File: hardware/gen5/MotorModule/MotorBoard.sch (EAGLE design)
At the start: 42 parts, among them J1 M20X2SHROUDED

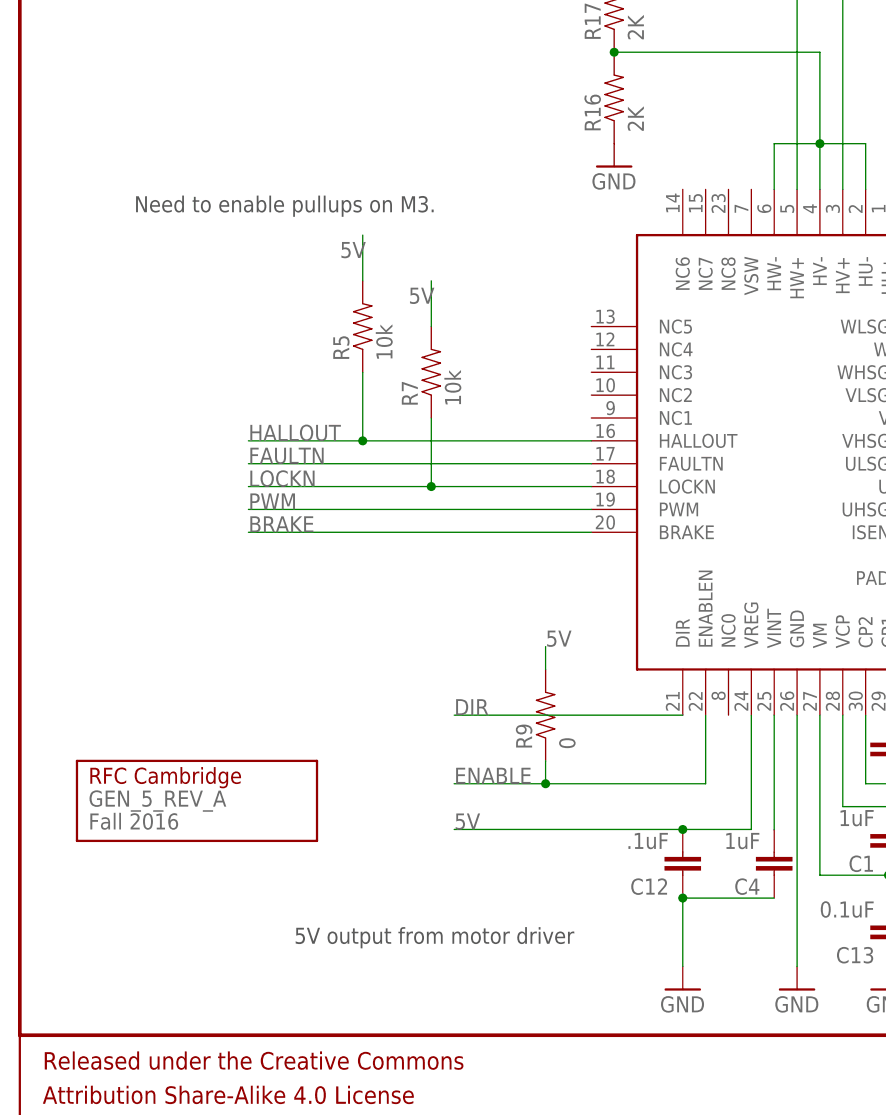
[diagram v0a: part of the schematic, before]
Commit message: added client code in rfc-ssl-vision-client
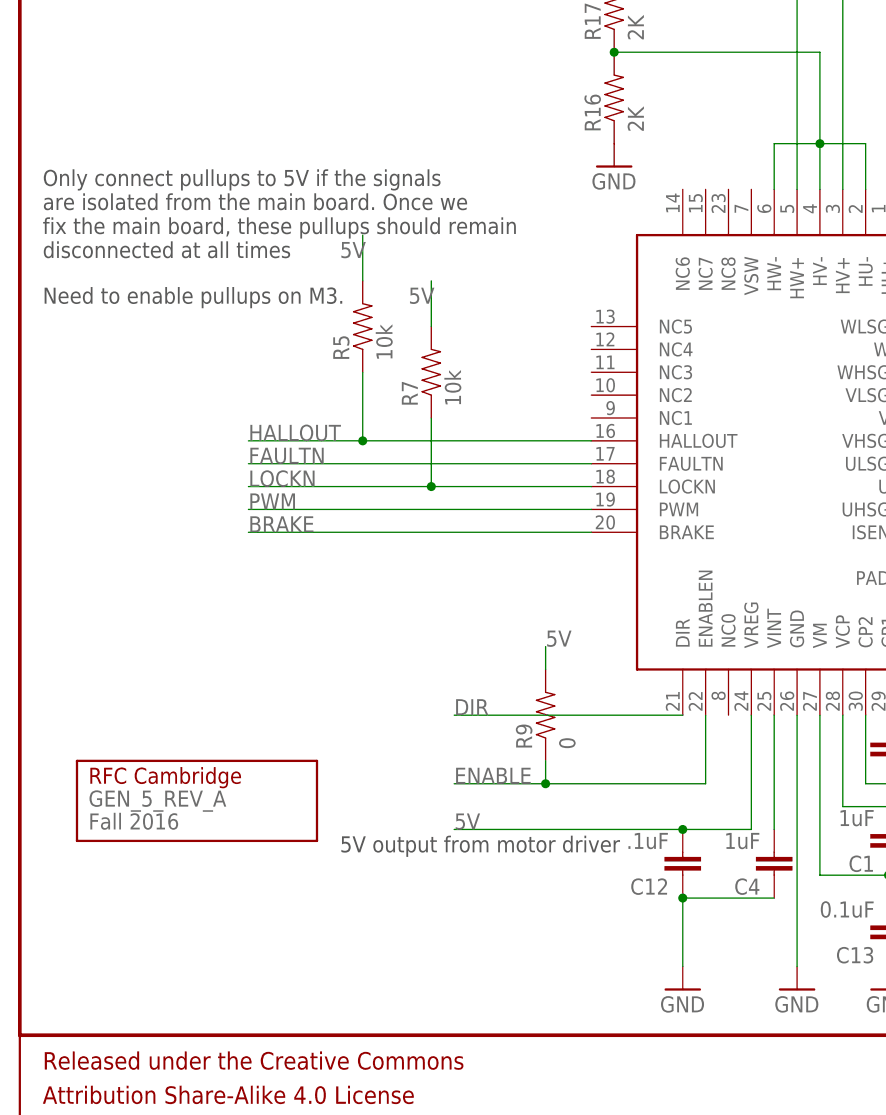
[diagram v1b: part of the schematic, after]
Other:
- note added: "Only connect pullups to 5V if the signals are isolated from the main board. Once we fix the main board, these pullups should remain disconnected at all times"
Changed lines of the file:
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@@
 <sheet>
 <plain>
-<text x="30.48" y="10.16" size="1.778" layer="97">5V output from motor driver</text>
+<text x="35.56" y="20.32" size="1.778" layer="97">5V output from motor driver</text>
 <text x="157.48" y="55.88" size="1.778" layer="97">Need to connect these with high current</text>
 <text x="157.48" y="53.34" size="1.778" layer="97">Separate connector?</text>
 <text x="254" y="81.28" size="1.778" layer="97">24, 26, and 30 are unconnected in Rev A</text>
-<text x="12.7" y="91.44" size="1.778" layer="97">Need to enable pullups on M3.</text>
+<text x="2.54" y="81.28" size="1.778" layer="97">Need to enable pullups on M3.</text>
+<text x="2.54" y="86.36" size="1.778" layer="97">Only connect pullups to 5V if the signals
+are isolated from the main board. Once we
+fix the main board, these pullups should remain
+disconnected at all times</text>
 </plain>
 <instances>
@@
 </schematic>
 </drawing>
+<compatibility>
+<note version="6.3" minversion="6.2.2" severity="warning">
+Since Version 6.2.2 text objects can contain more than one line,
+which will not be processed correctly with this version.
+</note>
+</compatibility>
 </eagle>

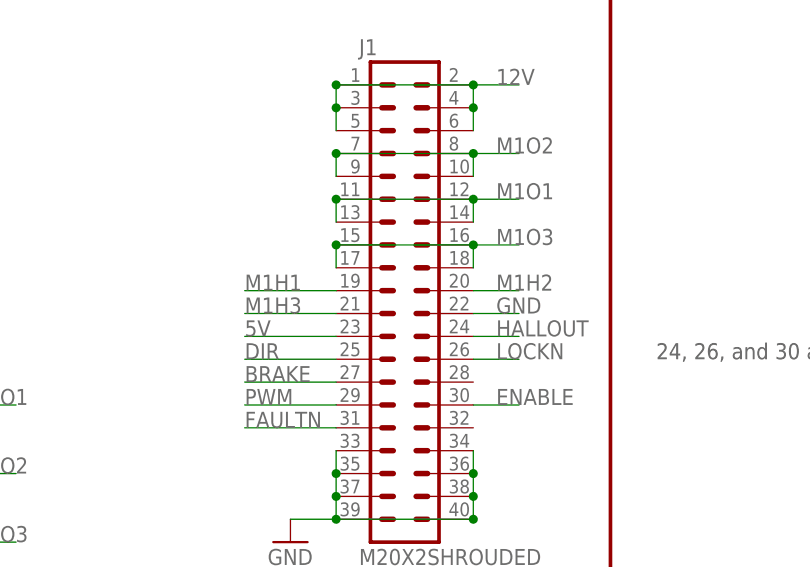
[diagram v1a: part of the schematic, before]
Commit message: swapped motorboard traces for hallout signals
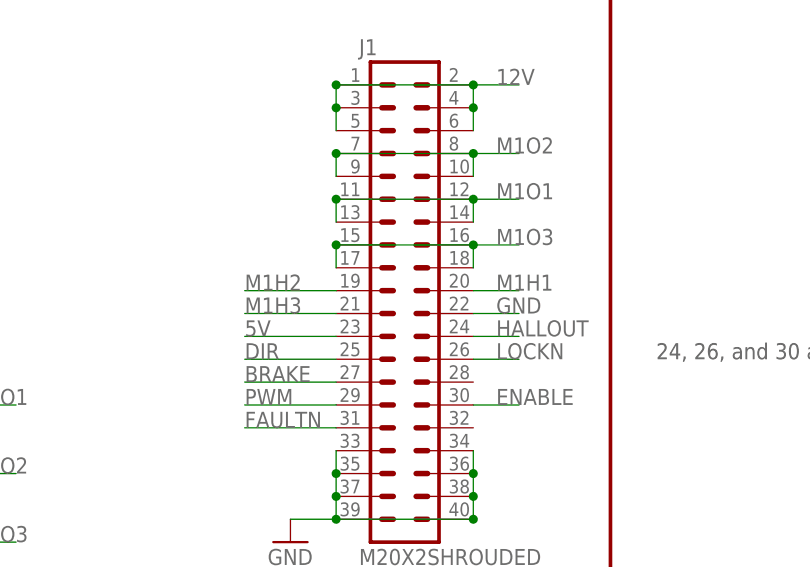
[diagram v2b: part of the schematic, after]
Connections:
- net M1H1: now also J1.20; no longer J1.19
- net M1H2: now also J1.19; no longer J1.20
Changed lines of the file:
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@@
-</segment>
-<segment>
-<pinref part="J1" gate="G$1" pin="20"/>
-<wire x1="233.68" y1="88.9" x2="238.76" y2="88.9" width="0.1524" layer="91"/>
-<label x="236.22" y="88.9" size="1.778" layer="95"/>
 </segment>
 <segment>
@@
 <wire x1="215.9" y1="129.54" x2="215.9" y2="121.92" width="0.1524" layer="91"/>
 <label x="215.9" y="121.92" size="1.778" layer="95" rot="R90"/>
+</segment>
+<segment>
+<pinref part="J1" gate="G$1" pin="19"/>
+<wire x1="218.44" y1="88.9" x2="208.28" y2="88.9" width="0.1524" layer="91"/>
+<label x="208.28" y="88.9" size="1.778" layer="95"/>
 </segment>
 </net>
@@
 </segment>
 <segment>
-<pinref part="J1" gate="G$1" pin="19"/>
-<wire x1="218.44" y1="88.9" x2="208.28" y2="88.9" width="0.1524" layer="91"/>
-<label x="208.28" y="88.9" size="1.778" layer="95"/>
-</segment>
-<segment>
 <pinref part="R3" gate="G$1" pin="2"/>
 <wire x1="208.28" y1="129.54" x2="208.28" y2="121.92" width="0.1524" layer="91"/>
 <label x="208.28" y="121.92" size="1.778" layer="95" rot="R90"/>
 </segment>
+<segment>
+<pinref part="J1" gate="G$1" pin="20"/>
+<wire x1="233.68" y1="88.9" x2="238.76" y2="88.9" width="0.1524" layer="91"/>
+<label x="236.22" y="88.9" size="1.778" layer="95"/>
+</segment>
 </net>

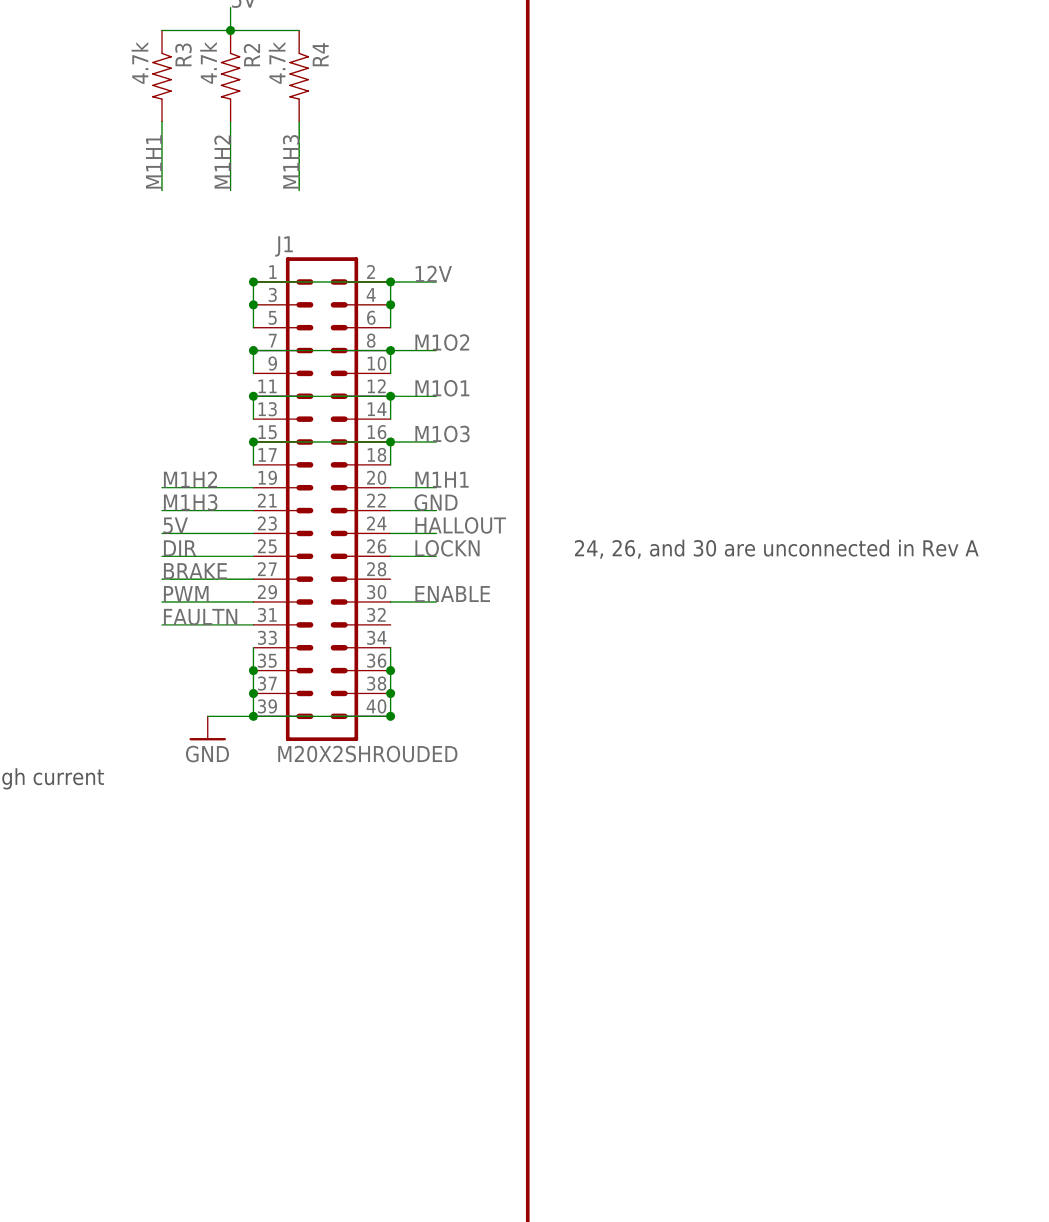
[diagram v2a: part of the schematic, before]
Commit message: starting to re-write motorboard
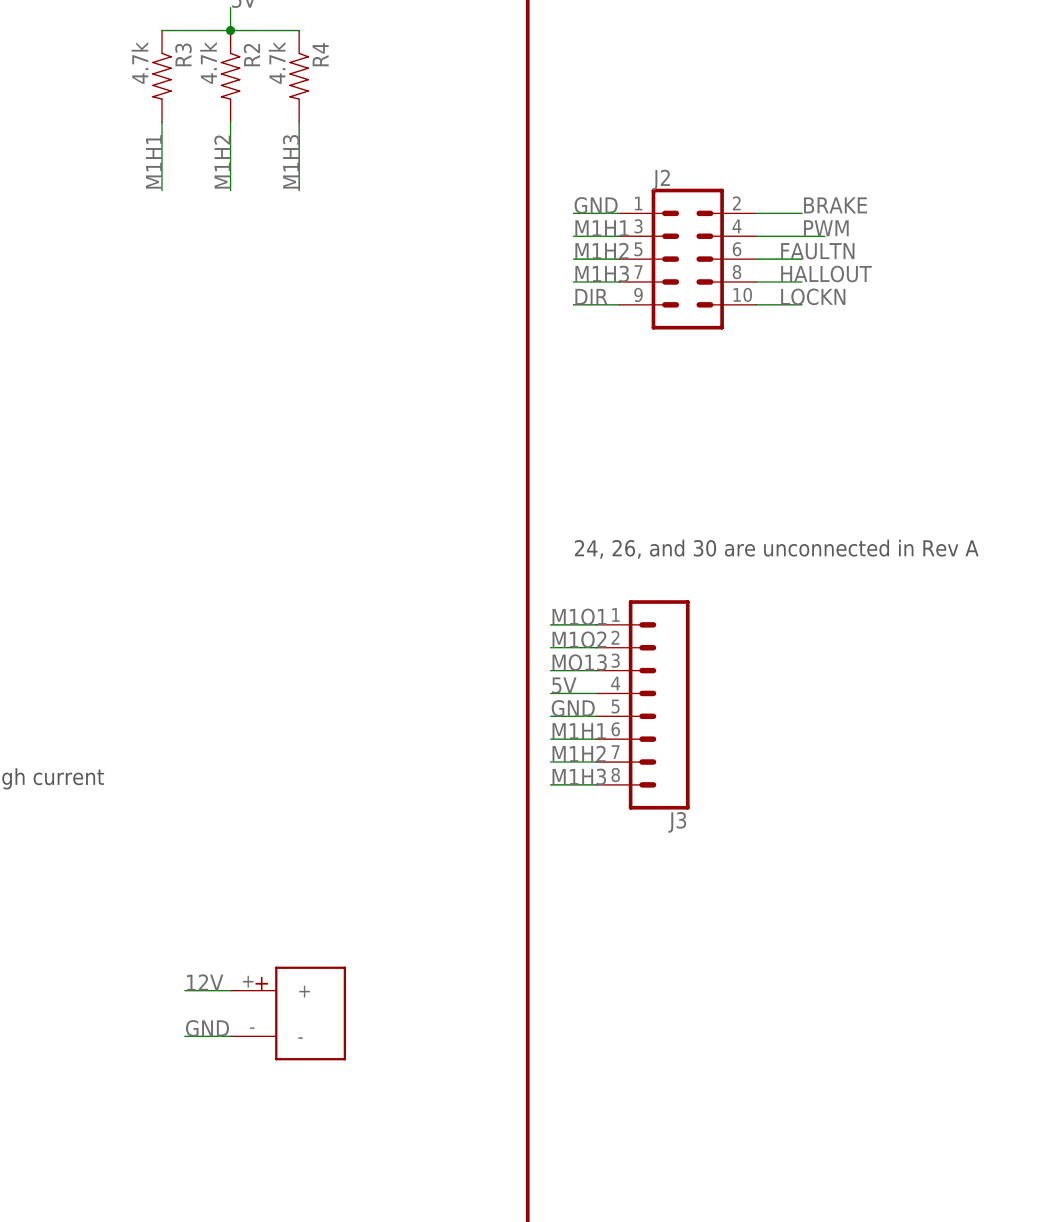
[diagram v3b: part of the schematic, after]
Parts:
- removed J1: M20X2SHROUDED, SparkFun-Connectors:M20X2SHROUDED
- added J2: (no value), SparkFun-Connectors:CONN_05X2SHD
- added J3: (no value), SparkFun-Connectors:CONN_08LONGPADS
- added U$2: CONN-POWER, Kicker:CONN-POWER
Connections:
- new net MO13: J3.3
- net 12V: now also U$2.+; no longer J1.1, J1.2, J1.3, J1.4, J1.5, J1.6
- net 5V: now also J3.4; no longer J1.23
- net BRAKE: now also J2.2; no longer J1.27
- net DIR: now also J2.9; no longer J1.25
- net ENABLE: no longer J1.30
- net FAULTN: now also J2.6; no longer J1.31
- net GND: now also J2.1, J3.5, U$2.-; no longer J1.22, J1.33, J1.34, J1.35, J1.36, J1.37, J1.38, J1.39, J1.40
- net HALLOUT: now also J2.8; no longer J1.24
- net LOCKN: now also J2.10; no longer J1.26
- net M1H1: now also J2.3, J3.6; no longer J1.20
- net M1H2: now also J2.5, J3.7; no longer J1.19
- net M1H3: now also J2.7, J3.8; no longer J1.21
- net M1O1: now also J3.1; no longer J1.11, J1.12, J1.13, J1.14
- net M1O2: now also J3.2; no longer J1.10, J1.7, J1.8, J1.9
- net M1O3: no longer J1.15, J1.16, J1.17, J1.18
- net PWM: now also J2.4; no longer J1.29

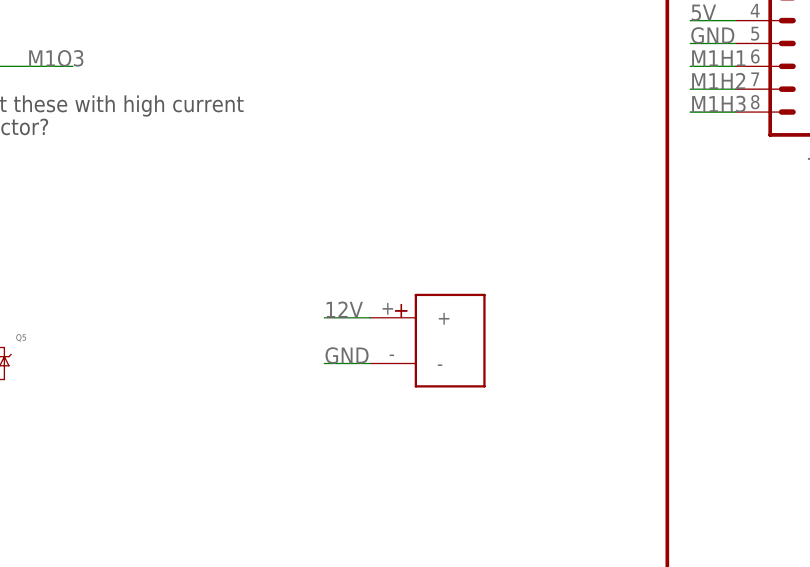
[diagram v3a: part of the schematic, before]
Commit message: added power connector to library and motorboard
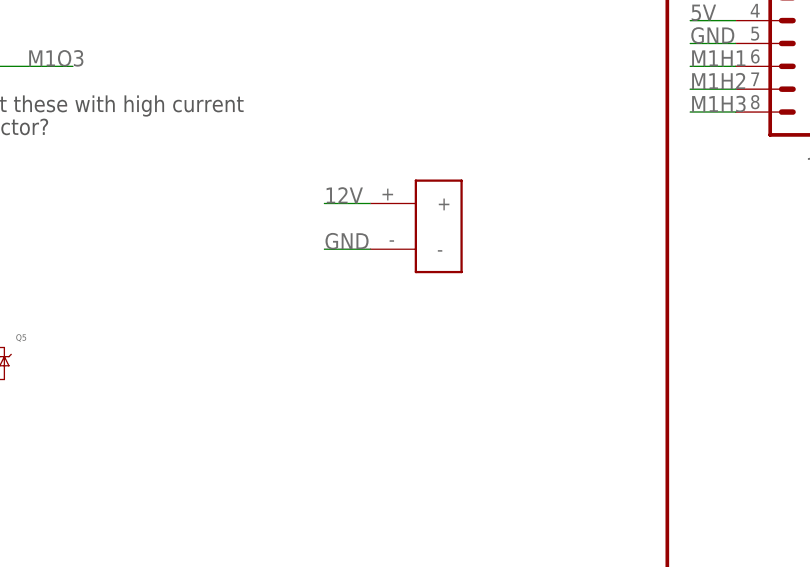
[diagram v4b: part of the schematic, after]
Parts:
- removed U$2: CONN-POWER, Kicker:CONN-POWER
- added U$3: POWER_CONN_2X1, Kicker:POWER_CONN_2X1
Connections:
- net 12V: now also U$3.+; no longer U$2.+
- net GND: now also U$3.-; no longer U$2.-
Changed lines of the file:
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@@
 <part name="R7" library="SparkFun-Resistors" deviceset="RESISTOR" device="0805-RES" value="10k"/>
 <part name="R9" library="SparkFun-Resistors" deviceset="RESISTOR" device="0805-RES" value="0"/>
-<part name="U$2" library="Kicker" deviceset="CONN-POWER" device=""/>
 <part name="J2" library="SparkFun-Connectors" library_urn="urn:adsk.eagle:library:513" deviceset="CONN_05X2" device="SHD" package3d_urn="urn:adsk.eagle:package:38000/1"/>
 <part name="J3" library="SparkFun-Connectors" library_urn="urn:adsk.eagle:library:513" deviceset="CONN_08" device="LONGPADS" package3d_urn="urn:adsk.eagle:package:38142/1"/>
+<part name="U$3" library="Kicker" deviceset="POWER_CONN_2X1" device=""/>
 </parts>
 <sheets>
@@
 <instance part="R7" gate="G$1" x="45.72" y="73.66" rot="R90"/>
 <instance part="R9" gate="G$1" x="58.42" y="35.56" rot="R90"/>
-<instance part="U$2" gate="G$1" x="220.98" y="30.48"/>
 <instance part="J2" gate="G$1" x="266.7" y="114.3"/>
 <instance part="J3" gate="G$1" x="261.62" y="66.04" rot="R180"/>
+<instance part="U$3" gate="G$1" x="223.52" y="43.18"/>
 </instances>
 <busses>
@@
 </segment>
 <segment>
-<pinref part="U$2" gate="G$1" pin="-"/>
-<wire x1="215.9" y1="27.94" x2="210.82" y2="27.94" width="0.1524" layer="91"/>
-<label x="210.82" y="27.94" size="1.778" layer="95"/>
-</segment>
-<segment>
 <pinref part="J2" gate="G$1" pin="1"/>
 <wire x1="259.08" y1="119.38" x2="254" y2="119.38" width="0.1524" layer="91"/>
@@
 <wire x1="256.54" y1="63.5" x2="251.46" y2="63.5" width="0.1524" layer="91"/>
 <label x="251.46" y="63.5" size="1.778" layer="95"/>
+</segment>
+<segment>
+<pinref part="U$3" gate="G$1" pin="-"/>
+<wire x1="215.9" y1="40.64" x2="210.82" y2="40.64" width="0.1524" layer="91"/>
+<label x="210.82" y="40.64" size="1.778" layer="95"/>
 </segment>
 </net>
@@
 </segment>
 <segment>
-<pinref part="U$2" gate="G$1" pin="+"/>
-<wire x1="215.9" y1="33.02" x2="210.82" y2="33.02" width="0.1524" layer="91"/>
-<label x="210.82" y="33.02" size="1.778" layer="95"/>
+<pinref part="U$3" gate="G$1" pin="+"/>
+<wire x1="215.9" y1="45.72" x2="210.82" y2="45.72" width="0.1524" layer="91"/>
+<label x="210.82" y="45.72" size="1.778" layer="95"/>
 </segment>
 </net>
